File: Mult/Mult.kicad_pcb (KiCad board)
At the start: 2 copper layers, 10.2 x 102.9 mm, 5 parts, among them J1 IN, J2 OUT1, J3 OUT2, J4 OUT3, J5 OUT4

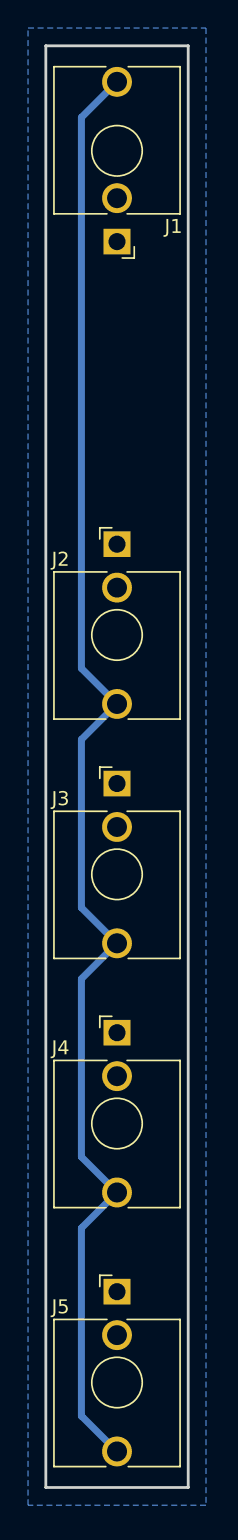
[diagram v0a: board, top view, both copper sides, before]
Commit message: add footprint model
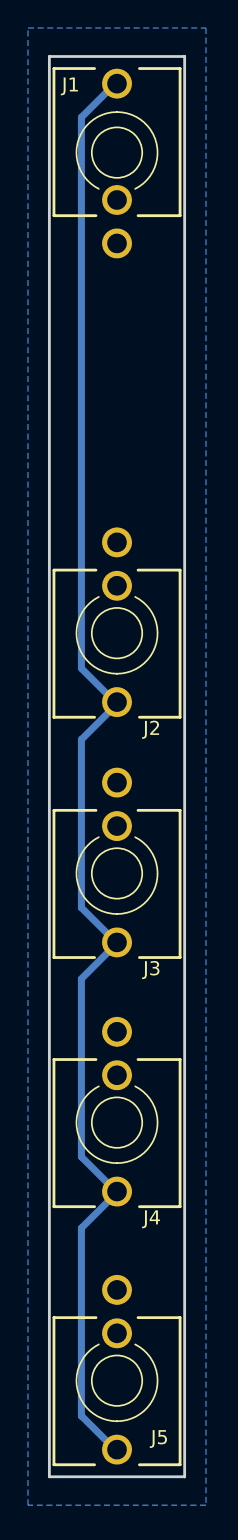
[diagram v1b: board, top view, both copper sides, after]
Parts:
- J1, J2, J3, J4, J5: footprint Connector_Audio:Jack_3.5mm_QingPu_WQP-PJ398SM_Vertical_CircularHoles -> pj398m:Jack_3.5mm_QingPu_WQP-PJ398SM_Vertical
- moved J4 6.42 mm to (152.4, 130.2), turned to 180 degrees
- moved J3 6.41 mm to (152.4, 112.4), turned to 180 degrees
- moved J1 6.35 mm to (152.4, 61.0), turned to 0 degrees
- moved J2 6.35 mm to (152.4, 95.2), turned to 180 degrees
- moved J5 6.35 mm to (152.4, 148.6), turned to 180 degrees
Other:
- board size 10.2 x 102.9 mm -> 9.7 x 101.3 mm

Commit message: fix component step files
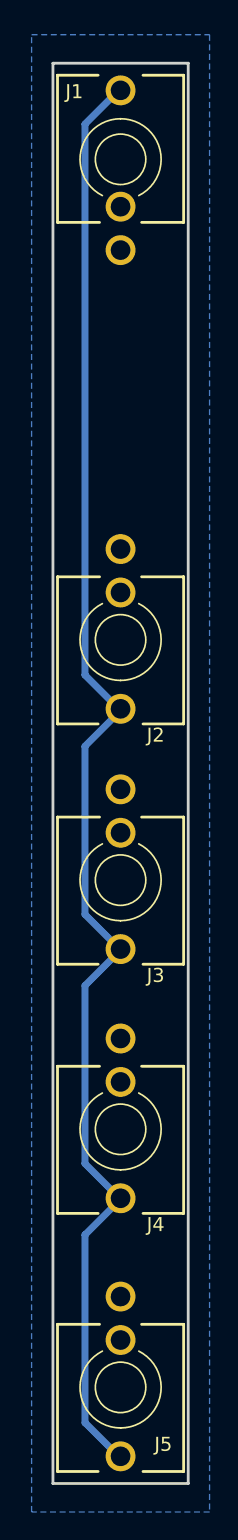
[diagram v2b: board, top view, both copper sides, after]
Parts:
- moved J3 0.54 mm to (152.7, 112.9)
- moved J5 0.54 mm to (152.7, 149.1)
- moved J1 0.54 mm to (152.7, 61.4)
- moved J2 0.54 mm to (152.7, 95.7)
- moved J4 0.54 mm to (152.7, 130.7)

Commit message: rearrange a bunch of files
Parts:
- moved J4 0.64 mm to (152.7, 131.3)
- moved J3 0.63 mm to (152.7, 113.5)
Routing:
- net Net-(J1-PadT): track 106.1 -> 105.6 mm
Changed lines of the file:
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@@
     (grid_origin 147.828 54.58)
     (pcbplotparams
-      (layerselection 0x00010fc_ffffffff)
+      (layerselection 0x0001000_fffffffe)
       (disableapertmacros false)
       (usegerberextensions false)
@@
       (viasonmask false)
       (mode 1)
-      (useauxorigin false)
+      (useauxorigin true)
       (hpglpennumber 1)
       (hpglpenspeed 20)
@@
       (outputformat 1)
       (mirror false)
-      (drillshape 1)
+      (drillshape 0)
       (scaleselection 1)
       (outputdirectory "")
@@
   )
   (footprint "pj398m:Jack_3.5mm_QingPu_WQP-PJ398SM_Vertical" (layer "F.Cu")
-    (at 152.654 112.873 180)
+    (at 152.654 113.508 180)
     (descr "T-S-SN Vertical mount jack AKA WQP-WQP518MA or Thonkiconn")
     (tags "WQP-WQP518MA, Thonkiconn")
@@
   )
   (footprint "pj398m:Jack_3.5mm_QingPu_WQP-PJ398SM_Vertical" (layer "F.Cu")
-    (at 152.654 130.653 180)
+    (at 152.654 131.288 180)
     (descr "T-S-SN Vertical mount jack AKA WQP-WQP518MA or Thonkiconn")
     (tags "WQP-WQP518MA, Thonkiconn")
@@
   (gr_line (start 147.828 155.926) (end 147.828 54.58) (layer "Edge.Cuts") (width 0.2))
   (gr_line (start 157.48 54.58) (end 157.48 155.926) (layer "Edge.Cuts") (width 0.2))
-  (segment (start 150.114 133.098) (end 150.114 120.398) (width 0.5) (layer "B.Cu") (net 2))
-  (segment (start 152.654 117.858) (end 150.114 120.398) (width 0.5) (layer "B.Cu") (net 2))
+  (dimension (type aligned) (layer "User.1")
+    (pts (xy 152.654 61.438) (xy 152.654 54.58))
+    (height -7.366)
+    (gr_text "6.8580 mm" (at 144.138 58.009 90) (layer "User.1")
+      (effects (font (size 1 1) (thickness 0.15)))
+    )
+    (format (units 3) (units_format 1) (precision 4))
+    (style (thickness 0.1) (arrow_length 1.27) (text_position_mode 0) (extension_height 0.58642) (extension_offset 0.5) keep_text_aligned)
+  )
+  (dimension (type aligned) (layer "User.1")
+    (pts (xy 152.654 149.048) (xy 152.654 54.58))
+    (height 10.414)
+    (gr_text "94.4680 mm" (at 161.918 101.814 90) (layer "User.1")
+      (effects (font (size 1 1) (thickness 0.15)))
+    )
+    (format (units 3) (units_format 1) (precision 4))
+    (style (thickness 0.1) (arrow_length 1.27) (text_position_mode 0) (extension_height 0.58642) (extension_offset 0.5) keep_text_aligned)
+  )
+  (dimension (type aligned) (layer "User.1")
+    (pts (xy 152.654 151.098) (xy 147.828 151.1))
+    (height -12.701051)
+    (gr_text "4.8260 mm" (at 150.245787 162.65005 0.02374462339) (layer "User.1")
+      (effects (font (size 1 1) (thickness 0.15)))
+    )
+    (format (units 3) (units_format 1) (precision 4))
+    (style (thickness 0.1) (arrow_length 1.27) (text_position_mode 0) (extension_height 0.58642) (extension_offset 0.5) keep_text_aligned)
+  )
+  (dimension (type orthogonal) (layer "User.1")
+    (pts (xy 152.654 149.068) (xy 152.654 131.288))
+    (height 18.034)
+    (orientation 1)
+    (gr_text "17.7800 mm" (at 169.538 140.178 90) (layer "User.1")
+      (effects (font (size 1 1) (thickness 0.15)))
+    )
+    (format (units 3) (units_format 1) (precision 4))
+    (style (thickness 0.15) (arrow_length 1.27) (text_position_mode 0) (extension_height 0.58642) (extension_offset 0.5) keep_text_aligned)
+  )
+  (segment (start 150.144 138.718) (end 152.654 136.208) (width 0.5) (layer "B.Cu") (net 2))
+  (segment (start 150.423318 120.658682) (end 152.654 118.428) (width 0.5) (layer "B.Cu") (net 2))
   (segment (start 152.654 100.778) (end 150.114 98.238) (width 0.5) (layer "B.Cu") (net 2))
+  (segment (start 150.423318 102.878682) (end 150.423318 116.197318) (width 0.5) (layer "B.Cu") (net 2))
   (segment (start 150.114 98.238) (end 150.114 58.928) (width 0.5) (layer "B.Cu") (net 2))
-  (segment (start 152.654 154.118) (end 150.144 151.608) (width 0.5) (layer "B.Cu") (net 2))
-  (segment (start 152.654 135.638) (end 150.114 138.178) (width 0.5) (layer "B.Cu") (net 2))
-  (segment (start 150.114 115.318) (end 150.114 103.318) (width 0.5) (layer "B.Cu") (net 2))
   (segment (start 150.114 58.928) (end 152.654 56.388) (width 0.5) (layer "B.Cu") (net 2))
-  (segment (start 150.114 103.318) (end 152.654 100.778) (width 0.5) (layer "B.Cu") (net 2))
-  (segment (start 150.144 151.608) (end 150.114 151.608) (width 0.5) (layer "B.Cu") (net 2))
-  (segment (start 152.654 135.638) (end 150.114 133.098) (width 0.5) (layer "B.Cu") (net 2))
-  (segment (start 150.114 138.178) (end 150.114 151.578) (width 0.5) (layer "B.Cu") (net 2))
-  (segment (start 152.654 117.858) (end 150.114 115.318) (width 0.5) (layer "B.Cu") (net 2))
+  (segment (start 152.654 136.208) (end 150.423318 133.977318) (width 0.5) (layer "B.Cu") (net 2))
+  (segment (start 150.423318 133.977318) (end 150.423318 120.658682) (width 0.5) (layer "B.Cu") (net 2))
+  (segment (start 150.423318 116.197318) (end 152.654 118.428) (width 0.5) (layer "B.Cu") (net 2))
+  (segment (start 152.654 100.648) (end 150.423318 102.878682) (width 0.5) (layer "B.Cu") (net 2))
+  (segment (start 150.144 138.718) (end 150.144 151.478) (width 0.5) (layer "B.Cu") (net 2))
+  (segment (start 150.144 151.478) (end 152.654 153.988) (width 0.5) (layer "B.Cu") (net 2))
   (zone (net 1) (net_name "GND") (layer "B.Cu") (hatch edge 0.508)
     (connect_pads (clearance 0.508))
